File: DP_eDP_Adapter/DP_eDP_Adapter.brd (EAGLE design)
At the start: 50 x 50 mm, 25 parts, among them IC1 TLC5947XLP

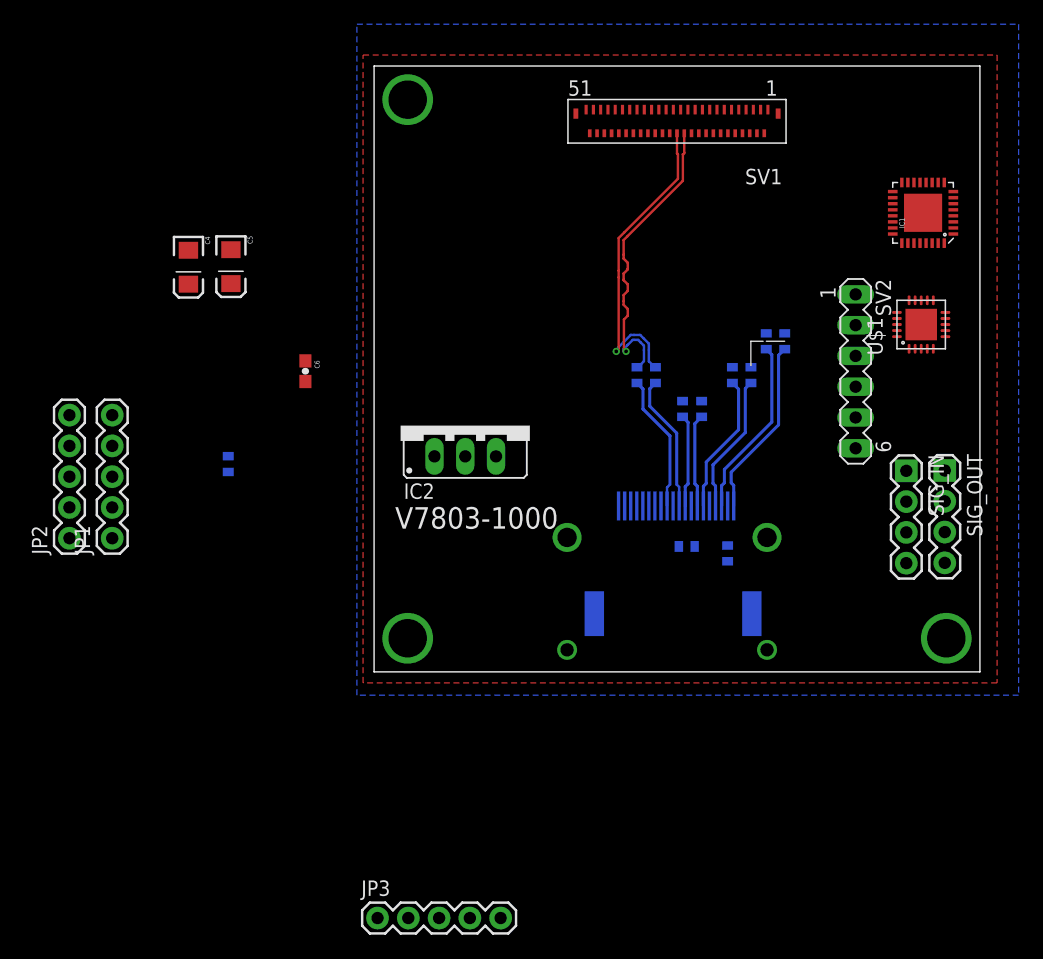
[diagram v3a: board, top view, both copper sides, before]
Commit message: 
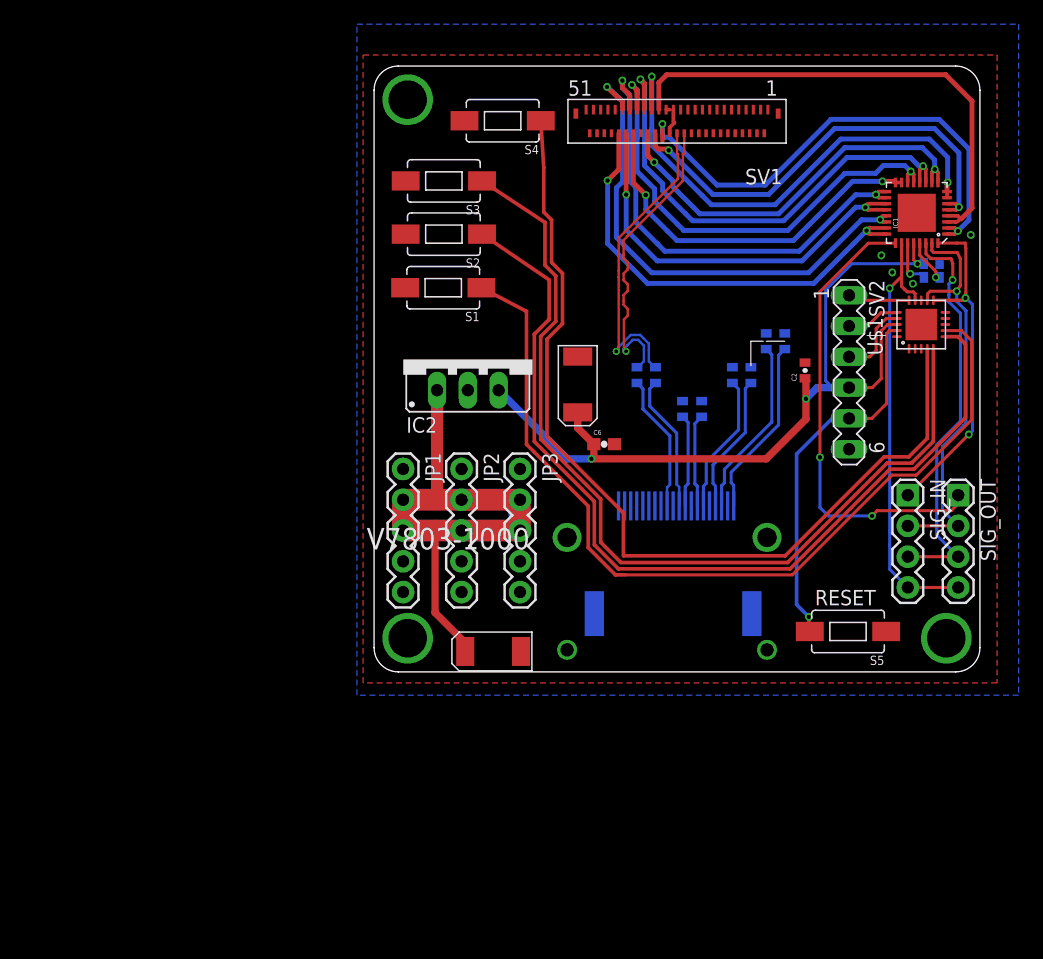
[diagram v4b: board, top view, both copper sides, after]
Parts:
- added S1, S2, S3, S4, S5: SWITCH-MOMENTARY-2-SMD-1101NE, SparkFun-Electromechanical:TACTILE-SWITCH-1101NE
- C4, C5: device SparkFun-Passives:EIA3216 -> SparkFun-Passives:EIA6032
- moved C2 48.2 mm to (10.6, -0.13), flipped to the top
- moved C4 40.5 mm to (-15.2, -23.3), turned to 0 degrees
- moved JP3 38.9 mm to (-13.0, -8.26), turned to 270 degrees
- moved JP2 32.9 mm to (-17.8, -8.26), turned to 270 degrees
- moved C1 30.9 mm to (21.0, 8.69), turned to 180 degrees
- moved C5 30.2 mm to (-8.19, -1.28), turned to 90 degrees
- moved R2 28.3 mm to (21.0, 7.56), turned to 0 degrees
- moved C6 25.4 mm to (-6.01, -6.21), turned to 0 degrees
- moved JP1 24.7 mm to (-22.6, -8.26), turned to 270 degrees
- moved IC2 5.47 mm to (-17.3, 0.79)
- moved SIG_OUT 2.31 mm to (23.2, -10.4)
- moved SIG_IN 2.01 mm to (19.1, -10.4)
- moved SV2 0.55 mm to (14.2, -0.27)
- moved IC1 0.52 mm to (19.8, 12.9)
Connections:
- removed net COL1: IC1.1
- removed net COL10: IC1.10
- removed net COL11: IC1.11
- removed net COL12: IC1.12
- removed net COL13: IC1.13
- removed net COL14: IC1.14
- removed net COL15: IC1.15
- removed net COL16: IC1.16
- removed net COL17: IC1.17
- removed net COL18: IC1.18
- removed net COL19: IC1.19
- removed net COL2: IC1.2
- removed net COL20: IC1.20
- removed net COL21: IC1.21
- removed net COL22: IC1.22
- removed net COL23: IC1.23
- removed net COL24: IC1.24
- removed net COL3: IC1.3
- removed net COL4: IC1.4
- removed net COL5: IC1.5
- removed net COL6: IC1.6
- removed net COL7: IC1.7
- removed net COL8: IC1.8
- removed net COL9: IC1.9
- removed net N$10: SV1.P$7
- removed net N$2: SV1.P$4
- removed net N$8: SV1.P$5
- removed net N$9: SV1.P$6
- new net BUTTON_1: S1.P$1, U$1.P$7
- new net BUTTON_2: S2.P$1, U$1.P$6
- new net BUTTON_3: S3.P$1, U$1.P$5
- new net BUTTON_4: S4.P$1, U$1.P$4
- new net VIN: SV1.P$4, SV1.P$5, SV1.P$6, SV1.P$7
- net +3V3: now also C5.P$1, IC2.OUT; no longer C5.A
- net 20V: now also C4.P$1, IC2.IN; no longer C4.A
- net GND: now also C4.P$2, C5.P$2, IC2.GND, S1.P$2, S2.P$2, S3.P$2, S4.P$2, S5.P$1; no longer C4.C, C5.C
- net LED_NEG_1A: now also IC1.23, IC1.24
- net LED_NEG_1B: now also IC1.11, IC1.12
- net LED_NEG_2A: now also IC1.21, IC1.22
- net LED_NEG_2B: now also IC1.10, IC1.9
- net LED_NEG_3A: now also IC1.19, IC1.20
- net LED_NEG_3B: now also IC1.7, IC1.8
- net LED_NEG_4A: now also IC1.17, IC1.18
- net LED_NEG_4B: now also IC1.5, IC1.6
- net LED_NEG_5A: now also IC1.15, IC1.16
- net LED_NEG_5B: now also IC1.3, IC1.4
- net LED_NEG_6A: now also IC1.13, IC1.14
- net LED_NEG_6B: now also IC1.1, IC1.2
- net RST: now also S5.P$2
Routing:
- net BUTTON_4: track 0.00 -> 76.2 mm
- net BUTTON_2: track 0.00 -> 75.7 mm
- net BUTTON_3: track 0.00 -> 75.5 mm
- net 20V: track 0.00 -> 72.9 mm
- net BUTTON_1: track 0.00 -> 72.7 mm
- net +3V3: track 0.00 -> 69.8 mm, vias 0 -> 3
- net LED_NEG_6B: track 0.00 -> 42.5 mm, vias 0 -> 2
- net LED_NEG_5B: track 0.00 -> 41.8 mm
- net LED_NEG_2A: track 0.00 -> 41.7 mm, vias 0 -> 2
- net LED_NEG_3B: track 0.00 -> 41.1 mm, vias 0 -> 2
- net LED_NEG_1B: track 0.00 -> 40.5 mm, vias 0 -> 2
- net LED_NEG_4A: track 0.00 -> 39.5 mm, vias 0 -> 2
- net LED_NEG_6A: track 0.00 -> 39.2 mm, vias 0 -> 2
- net SOUT: track 0.00 -> 38.5 mm, vias 0 -> 2
- net LED_NEG_1A: track 0.00 -> 37.5 mm, vias 0 -> 2
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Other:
- outline, holes or cut-outs redrawn
- board text added: "RESET"

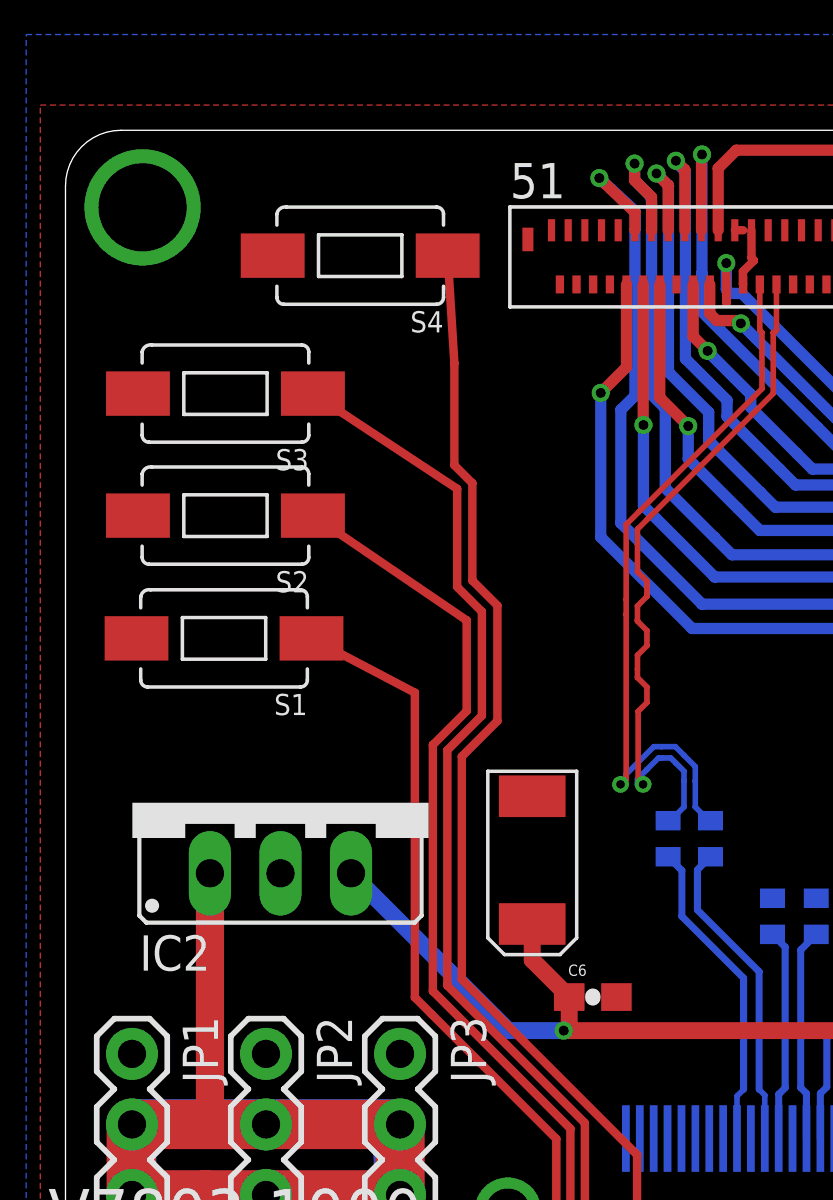
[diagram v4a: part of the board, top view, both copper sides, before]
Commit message: 
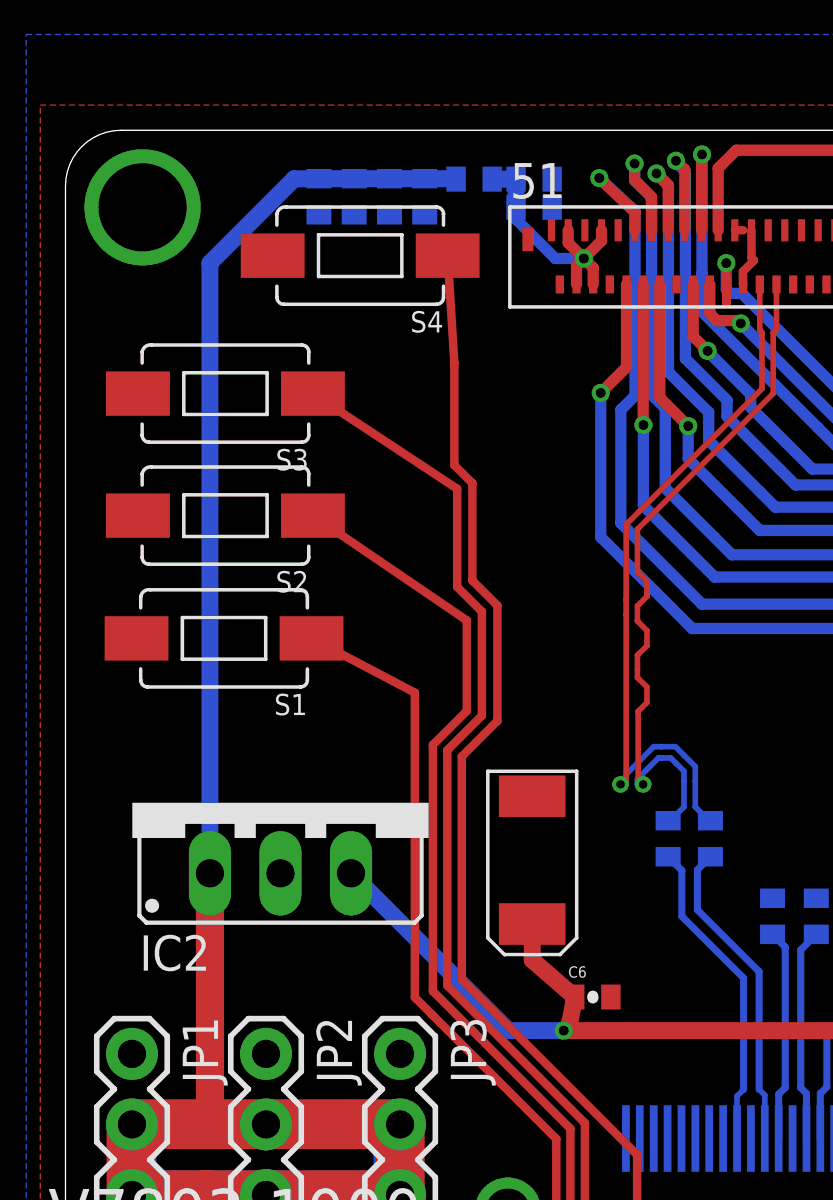
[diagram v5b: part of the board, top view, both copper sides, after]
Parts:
- added C14: .1uf, SparkFun-Passives:0402-CAP
- added C15: 0.1uF, SparkFun-Passives:0402-CAP
- added C16, C17: 82pF, SparkFun-Passives:0402-CAP
- added C18: 1000pF, SparkFun-Passives:0402-CAP
- added L1: (no value), rcl:R0402
- added R1: (no value), SparkFun-Passives:0402-RES
- C6: device SparkFun-Passives:0603-CAP -> SparkFun-Passives:0402-CAP
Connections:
- removed net LED_POS_1: SV1.P$48, SV1.P$49
- removed net LED_POS_2: SV1.P$45, SV1.P$46
- new net LED_POS: C17.1, C18.1, L1.2, SV1.P$45, SV1.P$46, SV1.P$48, SV1.P$49
- net 20V: now also C14.1, C15.1, C16.1, L1.1, R1.2
- net GND: now also C14.2, C15.2, C16.2, C17.2, C18.2, R1.1
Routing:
- net 20V: track 72.9 -> 105.0 mm
- net LED_POS: track 0.00 -> 9.98 mm, vias 0 -> 1
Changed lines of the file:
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@@
 <clearance class="1" value="0.2032"/>
+</class>
+<class number="2" name="Power" width="0.3048" drill="0">
 </class>
 </classes>
@@
 <element name="C4" library="SparkFun-Passives" package="EIA6032" value="10uF" x="-15.1758" y="-23.3131"/>
 <element name="C5" library="SparkFun-Passives" package="EIA6032" value="10uF" x="-8.1944" y="-1.2792" rot="R90"/>
-<element name="C6" library="SparkFun-Passives" package="0603-CAP" value=".1uf" x="-6.0124" y="-6.208"/>
+<element name="C6" library="SparkFun-Passives" package="0402-CAP" value=".1uf" x="-6.0124" y="-6.208"/>
 <element name="C2" library="SparkFun" package="0402-CAP" value="0.1uF" x="10.5664" y="-0.127" rot="R90"/>
 <element name="SIG_IN" library="SparkFun-Connectors" package="1X04" value="" x="19.05" y="-10.414" rot="R270"/>
@@
 <element name="S4" library="SparkFun-Electromechanical" package="TACTILE-SWITCH-1101NE" value="SWITCH-MOMENTARY-2-SMD-1101NE" x="-14.3891" y="20.4851" rot="R180"/>
 <element name="S5" library="SparkFun-Electromechanical" package="TACTILE-SWITCH-1101NE" value="SWITCH-MOMENTARY-2-SMD-1101NE" x="14.1097" y="-21.6662" rot="R180"/>
+<element name="C14" library="SparkFun-Passives" package="0402-CAP" value=".1uf" x="-15.875" y="22.606" rot="MR270"/>
+<element name="C15" library="SparkFun-Passives" package="0402-CAP" value="0.1uF" x="-14.605" y="22.606" rot="MR270"/>
+<element name="R1" library="SparkFun-Passives" package="0402-RES" value="" x="-13.335" y="22.606" rot="MR90"/>
+<element name="C16" library="SparkFun-Passives" package="0402-CAP" value="82pF" x="-12.065" y="22.606" rot="MR270"/>
+<element name="C17" library="SparkFun-Passives" package="0402-CAP" value="82pF" x="-8.128" y="23.241" rot="MR180"/>
+<element name="L1" library="rcl" package="R0402" value="" x="-10.287" y="23.241" rot="MR180"/>
+<element name="C18" library="SparkFun-Passives" package="0402-CAP" value="1000pF" x="-8.128" y="22.225" rot="MR180"/>
 </elements>
 <signals>
@@
 <contactref element="S5" pad="P$1"/>
 <via x="24.2443" y="11.0617" extent="1-16" drill="0.3556"/>
+<contactref element="C14" pad="2"/>
+<contactref element="C18" pad="2"/>
+<contactref element="C17" pad="2"/>
+<contactref element="C16" pad="2"/>
+<contactref element="R1" pad="1"/>
+<contactref element="C15" pad="2"/>
+<wire x1="-5.1" y1="21.4" x2="-7.5" y2="21.4" width="0" layer="19" extent="1-1"/>
 </signal>
 <signal name="SIN">
@@
 <wire x1="15.9078" y1="0.998" x2="14.1963" y2="0.998" width="0.254" layer="1"/>
 </signal>
-<signal name="20V">
+<signal name="20V" class="2">
 <contactref element="JP1" pad="3"/>
 <contactref element="JP1" pad="2"/>
@@
 <wire x1="-19.9644" y1="-20.1133" x2="-17.4758" y2="-22.6019" width="0.6096" layer="1"/>
 <wire x1="-17.4758" y1="-22.6019" x2="-17.4758" y2="-23.3131" width="0.6096" layer="1"/>
+<contactref element="C14" pad="1"/>
+<contactref element="C15" pad="1"/>
+<contactref element="R1" pad="2"/>
+<contactref element="C16" pad="1"/>
+<contactref element="L1" pad="1"/>
+<wire x1="-15.875" y1="23.256" x2="-14.605" y2="23.256" width="0.6096" layer="16"/>
+<wire x1="-14.605" y1="23.256" x2="-13.335" y2="23.256" width="0.6096" layer="16"/>
+<wire x1="-13.335" y1="23.256" x2="-12.065" y2="23.256" width="0.6096" layer="16"/>
+<wire x1="-12.065" y1="23.256" x2="-10.952" y2="23.256" width="0.6096" layer="16"/>
+<wire x1="-10.952" y1="23.256" x2="-10.937" y2="23.241" width="0.6096" layer="16"/>
+<wire x1="-19.7993" y1="-1.7526" x2="-19.7993" y2="20.2184" width="0.6096" layer="16"/>
+<wire x1="-19.7993" y1="20.2184" x2="-16.764" y2="23.2537" width="0.6096" layer="16"/>
+<wire x1="-16.764" y1="23.2537" x2="-15.8773" y2="23.2537" width="0.6096" layer="16"/>
+<wire x1="-15.8773" y1="23.2537" x2="-15.875" y2="23.256" width="0.6096" layer="16"/>
 <wire x1="-22.606" y1="-13.335" x2="-22.6314" y2="-13.3096" width="0" layer="19" extent="1-1"/>
 </signal>
@@
 <wire x1="10.6426" y1="-0.8532" x2="10.6426" y2="-2.4638" width="0.6096" layer="1"/>
 <wire x1="-7.0612" y1="-7.4168" x2="-6.8624" y2="-7.218" width="0.6096" layer="1"/>
-<wire x1="-6.8624" y1="-7.218" x2="-6.8624" y2="-6.208" width="0.6096" layer="1"/>
-<wire x1="-6.8624" y1="-6.208" x2="-8.1944" y2="-4.876" width="0.6096" layer="1"/>
+<wire x1="-6.8624" y1="-7.218" x2="-6.6624" y2="-6.208" width="0.6096" layer="1"/>
+<wire x1="-6.6624" y1="-6.208" x2="-8.1944" y2="-4.876" width="0.6096" layer="1"/>
 <wire x1="-8.1944" y1="-4.876" x2="-8.1944" y2="-3.5792" width="0.6096" layer="1"/>
 </signal>
@@
 <wire x1="22.9215" y1="11.6352" x2="23.1775" y2="11.3792" width="0.3048" layer="1"/>
 </signal>
-<signal name="LED_POS_2">
-<contactref element="SV1" pad="P$46"/>
-<contactref element="SV1" pad="P$45"/>
-<wire x1="-6" y1="19.45" x2="-5.7" y2="21.4" width="0" layer="19" extent="1-1"/>
-</signal>
-<signal name="LED_POS_1">
-<contactref element="SV1" pad="P$49"/>
-<contactref element="SV1" pad="P$48"/>
-<wire x1="-6.6" y1="19.45" x2="-6.9" y2="21.4" width="0" layer="19" extent="1-1"/>
-</signal>
 <signal name="N$3_P" class="1">
 <contactref element="C3" pad="1"/>
@@
 <wire x1="-10.9982" y1="16.612" x2="-11.2391" y2="20.4851" width="0.3048" layer="1"/>
 </signal>
+<signal name="LED_POS">
+<contactref element="SV1" pad="P$49"/>
+<contactref element="SV1" pad="P$48"/>
+<contactref element="SV1" pad="P$46"/>
+<contactref element="SV1" pad="P$45"/>
+<contactref element="L1" pad="2"/>
+<contactref element="C17" pad="1"/>
+<contactref element="C18" pad="1"/>
+<wire x1="-9.637" y1="23.241" x2="-8.778" y2="23.241" width="0.6096" layer="16"/>
+<wire x1="-8.778" y1="23.241" x2="-8.778" y2="22.225" width="0.6096" layer="16"/>
+<wire x1="-8.778" y1="22.225" x2="-8.778" y2="21.7955" width="0.4064" layer="16"/>
+<wire x1="-8.778" y1="21.7955" x2="-7.366" y2="20.3835" width="0.4064" layer="16"/>
+<wire x1="-7.366" y1="20.3835" x2="-6.3373" y2="20.3835" width="0.4064" layer="16"/>
+<via x="-6.3373" y="20.3835" extent="1-16" drill="0.3556"/>
+<wire x1="-6.3373" y1="20.3835" x2="-6.9" y2="20.9462" width="0.4064" layer="1"/>
+<wire x1="-6.9" y1="20.9462" x2="-6.9" y2="21.4" width="0.4064" layer="1"/>
+<wire x1="-6.3373" y1="20.3835" x2="-6.6" y2="20.1208" width="0.4064" layer="1"/>
+<wire x1="-6.6" y1="20.1208" x2="-6.6" y2="19.45" width="0.4064" layer="1"/>
+<wire x1="-6" y1="19.45" x2="-6" y2="20.0462" width="0.4064" layer="1"/>
+<wire x1="-6" y1="20.0462" x2="-6.3373" y2="20.3835" width="0.4064" layer="1"/>
+<wire x1="-5.7" y1="21.4" x2="-5.7" y2="21.0208" width="0.4064" layer="1"/>
+<wire x1="-5.7" y1="21.0208" x2="-6.3373" y2="20.3835" width="0.4064" layer="1"/>
+</signal>
 </signals>
